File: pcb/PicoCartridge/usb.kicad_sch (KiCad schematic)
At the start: 1 part, among them J2 USB_C_Receptacle_USB2.0_14P

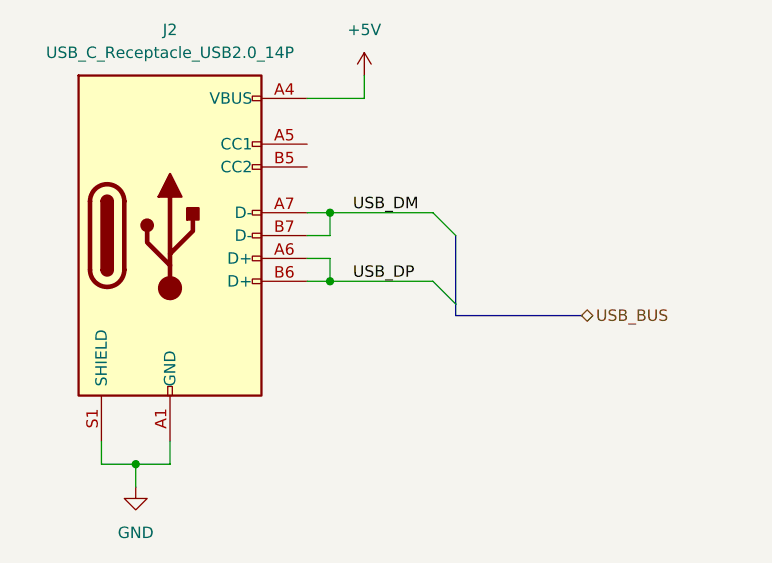
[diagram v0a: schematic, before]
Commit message: Defined additional interfaces
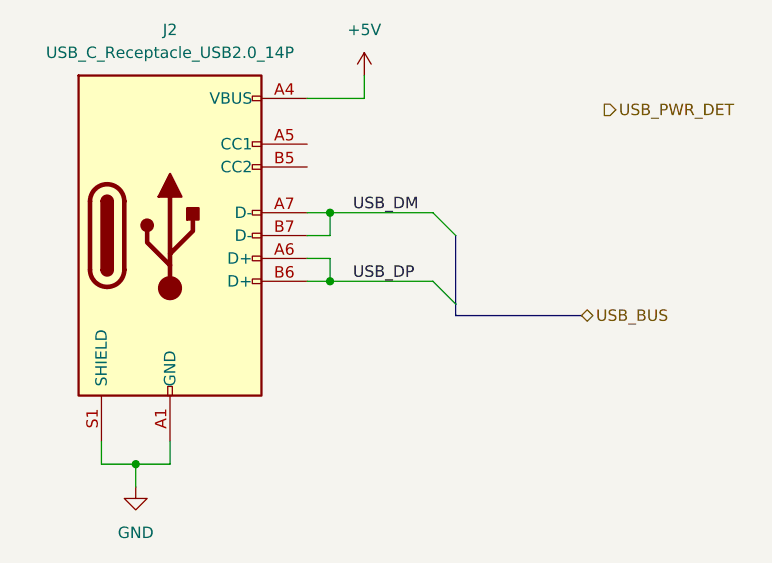
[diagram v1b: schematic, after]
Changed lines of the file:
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@@
+		)
+	)
+	(hierarchical_label "USB_PWR_DET"
+		(shape output)
+		(at 128.27 46.99 0)
+		(fields_autoplaced yes)
+		(effects
+			(font
+				(size 1.27 1.27)
+			)
+			(justify left)
 		)
 	)
